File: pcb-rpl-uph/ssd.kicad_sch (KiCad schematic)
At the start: 9 parts, among them J10 Bus_M.2_Socket_M

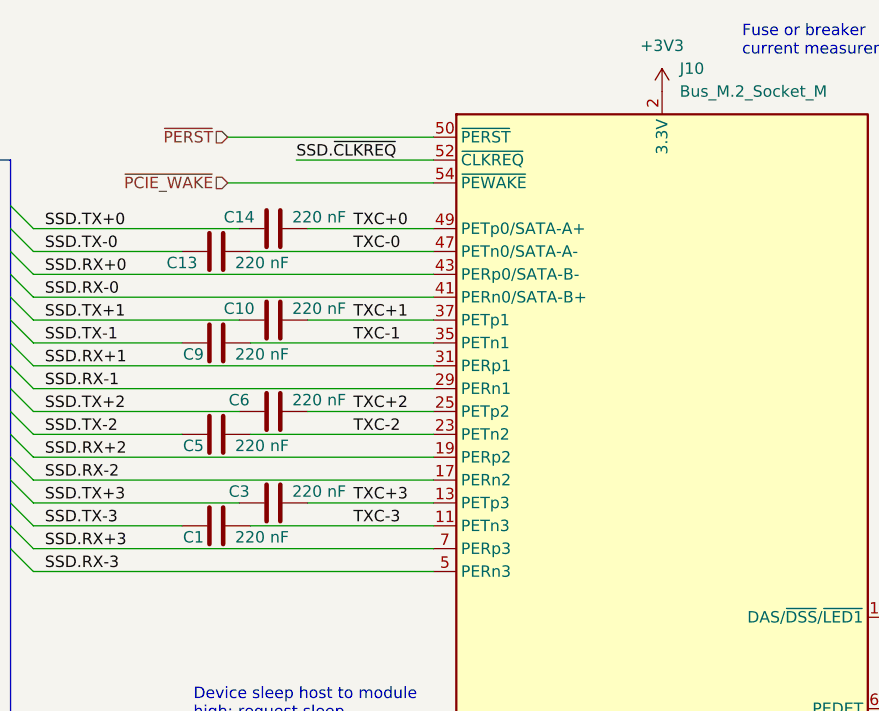
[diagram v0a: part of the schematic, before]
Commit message: Rename motherboard project, add models and footprints for M.2, USB-A, and USB-C
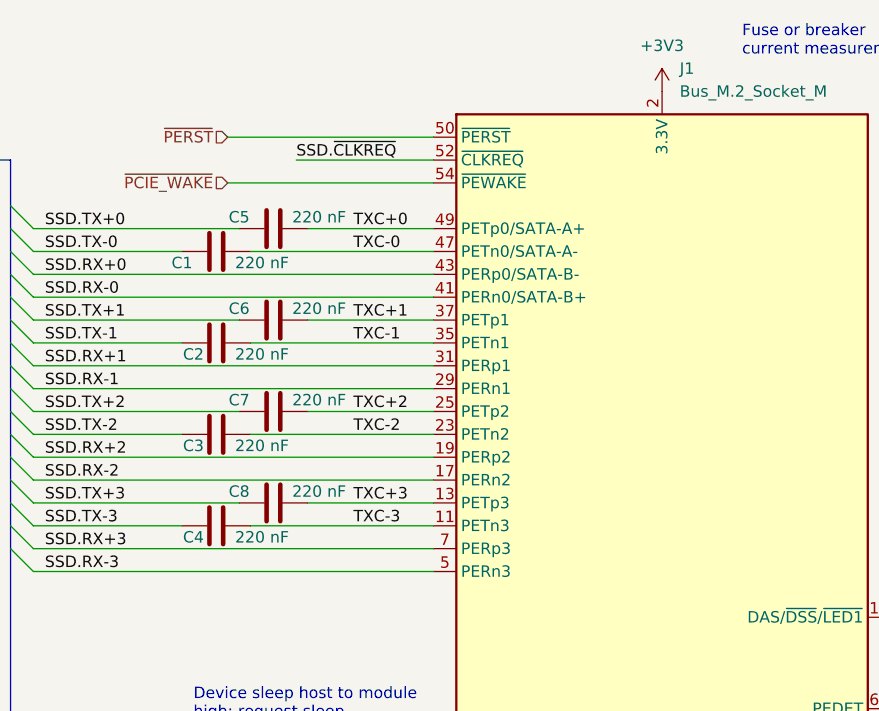
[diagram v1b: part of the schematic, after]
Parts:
- J1: renamed from J10; footprint nuc-12-carrier:M2_M -> local:M2_M
- renumbered C13 to C1, C9 to C2, C5 to C3, C1 to C4, C14 to C5, C10 to C6, C6 to C7, C3 to C8

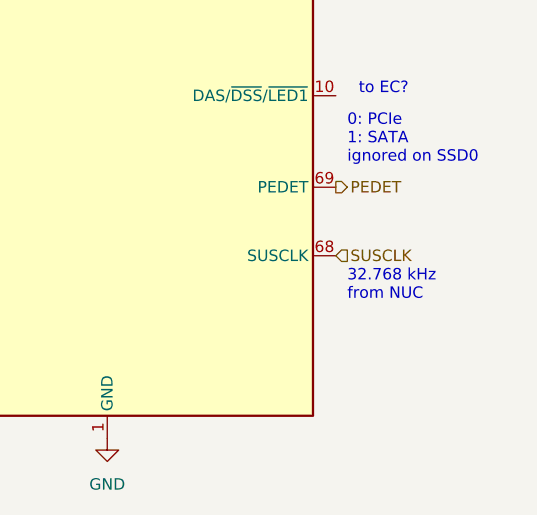
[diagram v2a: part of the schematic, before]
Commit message: refactor much of CPU schematic symbol
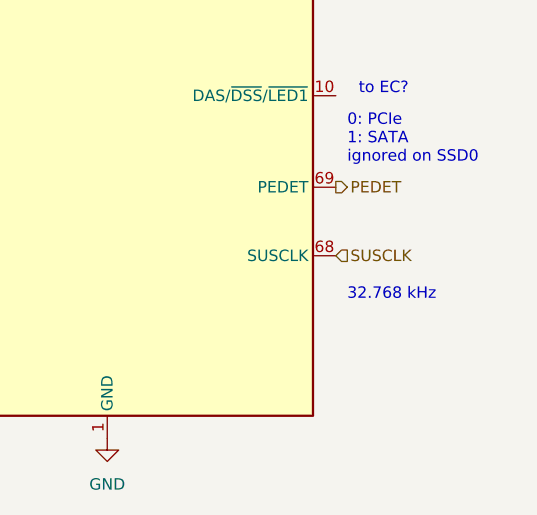
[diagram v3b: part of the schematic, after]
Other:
- note added: "32.768 kHz"
- note removed: "32.768 kHz from NUC"
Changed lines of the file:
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@@
     (effects (font (size 1.27 1.27)) (justify left bottom))
   )
-  (text "32.768 kHz\nfrom NUC" (at 198.12 125.73 0)
+  (text "32.768 kHz" (at 198.12 125.73 0)
     (effects (font (size 1.27 1.27)) (justify left bottom))
   )
